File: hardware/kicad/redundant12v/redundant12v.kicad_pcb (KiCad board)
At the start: 2 copper layers, 66.7 x 26.4 mm, 30 parts, among them J1 Conn_01x06, J2 IDC 2x5 Male, Q1 2N3904, Q2 2N3904, U1 ATtiny212-SS, U2 MAX232CPE, U3 LD1117S50TR_SOT223, X1 ASCO

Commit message: Replace Maxim MAX232ECWE+T with TI MAX232EID for narrower SOIC-16
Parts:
- C1, C2, C4, C8: value C_Small -> 0.1μF
- C3, C5, C6, C7: value C_Small -> 1μF
- C9: value C_Small -> 10μF
- D1: value BZX84Cxx -> BZX84-A15,215
- F1: value Fuse -> F1206B1R00FSTR
- J1: value Conn_01x06 -> 22-12-2064
- Q1, Q2: value 2N3904 -> SMMBT3904LT1G
- U1: value ATtiny212-SS -> ATTINY212-SSF
- U2: value MAX232CPE -> TI MAX232EID
- U3: value LD1117S50TR_SOT223 -> LD1117S50CTR
- X1: value ASCO -> ECS-3951M-018-AU-TR
- renumbered TP1 to TP3
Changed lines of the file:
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@@
       (effects (font (size 1 1) (thickness 0.15)))
     )
-    (fp_text value "C_Small" (at -4.625 -1.27 90) (layer "F.Fab")
+    (fp_text value "0.1μF" (at -4.625 -1.27 90) (layer "F.Fab")
       (effects (font (size 1 1) (thickness 0.15)))
     )
@@
       (effects (font (size 1 1) (thickness 0.15)))
     )
-    (fp_text value "C_Small" (at -1.2935 1.172) (layer "F.Fab")
+    (fp_text value "10μF" (at -1.2935 1.172) (layer "F.Fab")
       (effects (font (size 1 1) (thickness 0.15)))
     )
@@
       (effects (font (size 1 1) (thickness 0.15)))
     )
-    (fp_text value "C_Small" (at 0 1.68 90) (layer "F.Fab")
+    (fp_text value "1μF" (at 0 1.68 90) (layer "F.Fab")
       (effects (font (size 1 1) (thickness 0.15)))
     )
@@
       (effects (font (size 1 1) (thickness 0.15)))
     )
-    (fp_text value "Conn_01x06" (at 6.25 3.4 90) (layer "F.Fab")
+    (fp_text value "22-12-2064" (at 6.25 3.4 90) (layer "F.Fab")
       (effects (font (size 1 1) (thickness 0.15)))
     )
@@
       (effects (font (size 1 1) (thickness 0.15)))
     )
-    (fp_text value "C_Small" (at -0.27 -2.54 90) (layer "F.Fab")
+    (fp_text value "1μF" (at -0.27 -2.54 90) (layer "F.Fab")
       (effects (font (size 1 1) (thickness 0.15)))
     )
@@
       (effects (font (size 1 1) (thickness 0.15)))
     )
-    (fp_text value "Fuse" (at -0.4207 5.376) (layer "F.Fab")
+    (fp_text value "F1206B1R00FSTR" (at -0.4207 5.376) (layer "F.Fab")
       (effects (font (size 1 1) (thickness 0.15)))
     )
@@
       (effects (font (size 1 1) (thickness 0.15)))
     )
-    (fp_text value "2N3904" (at -2.866 0.293 90) (layer "F.Fab")
+    (fp_text value "SMMBT3904LT1G" (at -2.866 0.293 90) (layer "F.Fab")
       (effects (font (size 1 1) (thickness 0.15)))
     )
@@
       (effects (font (size 1 1) (thickness 0.15)))
     )
-    (fp_text value "ATtiny212-SS" (at 0 3.4 90) (layer "F.Fab")
+    (fp_text value "ATTINY212-SSF" (at 0 3.4 90) (layer "F.Fab")
       (effects (font (size 1 1) (thickness 0.15)))
     )
@@
       (effects (font (size 1 1) (thickness 0.15)))
     )
-    (fp_text value "MAX232CPE" (at 0 10.1285 90) (layer "F.Fab")
+    (fp_text value "TI MAX232EID" (at 0 10.1285 90) (layer "F.Fab")
       (effects (font (size 1 1) (thickness 0.15)))
     )
@@
       (effects (font (size 1 1) (thickness 0.15)))
     )
-    (fp_text value "ASCO" (at 0 5 90) (layer "F.Fab")
+    (fp_text value "ECS-3951M-018-AU-TR" (at 0 5 90) (layer "F.Fab")
       (effects (font (size 1 1) (thickness 0.15)))
     )
@@
       (effects (font (size 1 1) (thickness 0.15)))
     )
-    (fp_text value "LD1117S50TR_SOT223" (at 0.127 -5.334 90) (layer "F.Fab")
+    (fp_text value "LD1117S50CTR" (at 0.127 -5.334 90) (layer "F.Fab")
       (effects (font (size 1 1) (thickness 0.15)))
     )
@@
       (effects (font (size 1 1) (thickness 0.15)))
     )
-    (fp_text value "C_Small" (at -4.18 -12.9325) (layer "F.Fab")
+    (fp_text value "1μF" (at -4.18 -12.9325) (layer "F.Fab")
       (effects (font (size 1 1) (thickness 0.15)))
     )
@@
       (effects (font (size 1 1) (thickness 0.15)))
     )
-    (fp_text value "C_Small" (at -1.188 -2.8045 90) (layer "F.Fab")
+    (fp_text value "0.1μF" (at -1.188 -2.8045 90) (layer "F.Fab")
       (effects (font (size 1 1) (thickness 0.15)))
     )
@@
       (effects (font (size 1 1) (thickness 0.15)))
     )
-    (fp_text value "C_Small" (at 0 1.68 90) (layer "F.Fab")
+    (fp_text value "0.1μF" (at 0 1.68 90) (layer "F.Fab")
       (effects (font (size 1 1) (thickness 0.15)))
     )
@@
       (effects (font (size 1 1) (thickness 0.15)))
     )
-    (fp_text value "BZX84Cxx" (at 0 2.4 90) (layer "F.Fab")
+    (fp_text value "BZX84-A15,215" (at 0 2.4 90) (layer "F.Fab")
       (effects (font (size 1 1) (thickness 0.15)))
     )
@@
       (effects (font (size 1 1) (thickness 0.15)))
     )
-    (fp_text value "C_Small" (at 2.7755 1.742 90) (layer "F.Fab")
+    (fp_text value "1μF" (at 2.7755 1.742 90) (layer "F.Fab")
       (effects (font (size 1 1) (thickness 0.15)))
     )
@@
       (effects (font (size 1 1) (thickness 0.15)))
     )
-    (fp_text value "C_Small" (at -0.115 -0.559 90) (layer "F.Fab")
+    (fp_text value "0.1μF" (at -0.115 -0.559 90) (layer "F.Fab")
       (effects (font (size 1 1) (thickness 0.15)))
     )
@@
       (effects (font (size 1 1) (thickness 0.15)))
     )
-    (fp_text value "2N3904" (at 4.157 3.826) (layer "F.Fab")
+    (fp_text value "SMMBT3904LT1G" (at 4.157 3.826) (layer "F.Fab")
       (effects (font (size 1 1) (thickness 0.15)))
     )
@@
     (property "Sheetname" "")
     (attr exclude_from_pos_files)
-    (fp_text reference "TP1" (at 0 2.148) (layer "B.SilkS") hide
+    (fp_text reference "TP3" (at 0 2.148) (layer "B.SilkS") hide
       (effects (font (size 1 1) (thickness 0.15)) (justify mirror))
     )

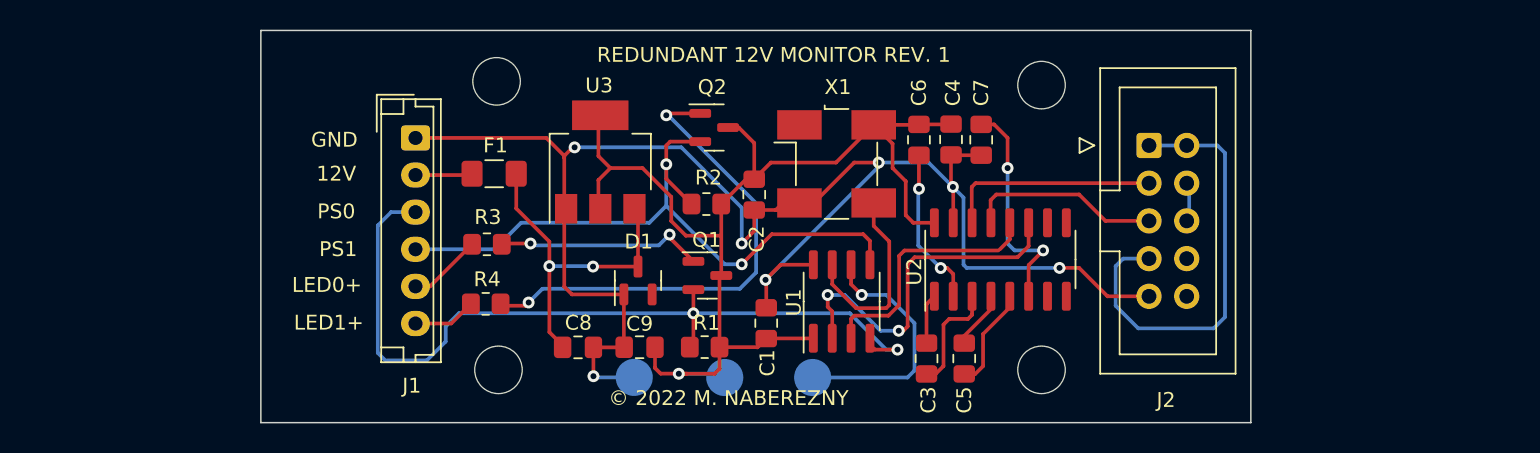
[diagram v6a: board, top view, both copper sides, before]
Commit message: Fix alarm detection, rotate serial connector
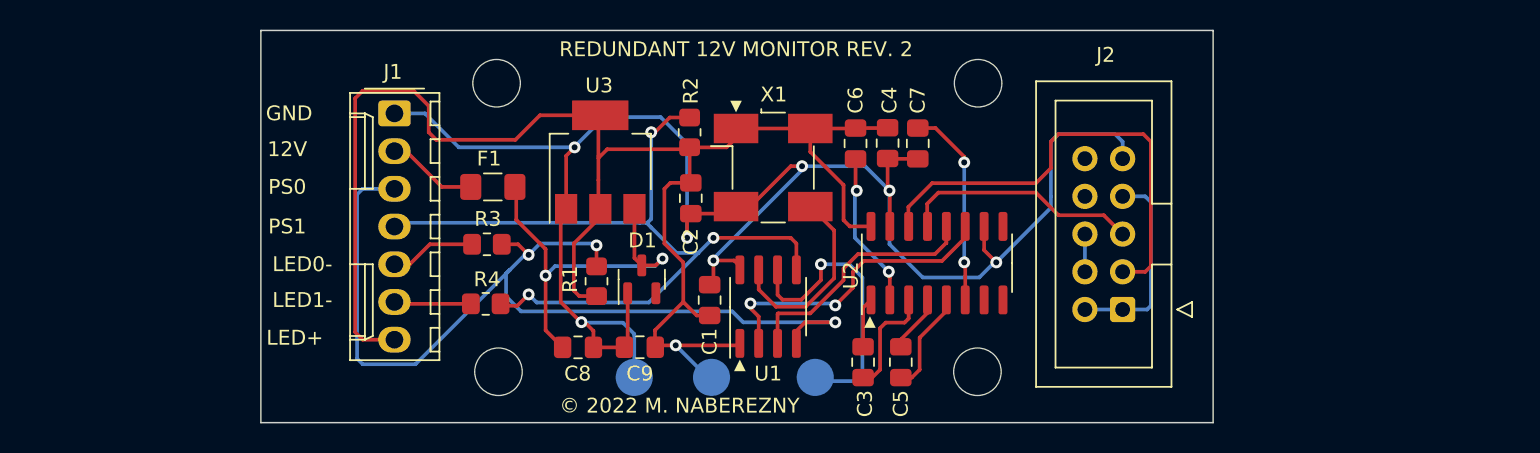
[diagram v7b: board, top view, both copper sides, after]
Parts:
- removed Q1, Q2: SMMBT3904LT1G, Package_TO_SOT_SMD:SOT-23
- J1: value 22-12-2064 -> Conn_01x07; footprint Connector_JST:JST_EH_B6B-EH-A_1x06_P2.50mm_Vertical -> Connector_Molex:Molex_KK-254_AE-6410-07A_1x07_P2.54mm_Vertical
- moved J2 11.2 mm to (176.1, 99.1), turned to 180 degrees
- moved R1 8.53 mm to (140.7, 97.2), turned to 90 degrees
- moved U1 4.97 mm to (152.3, 98.9)
- moved R2 4.96 mm to (147.0, 87.1), turned to 90 degrees
- moved REF** 4.32 mm to (166.4, 103.3)
- moved C3 4.28 mm to (158.7, 102.6)
- moved U2 4.28 mm to (163.6, 95.9)
- moved C4 4.28 mm to (160.3, 87.9)
- moved C5 4.28 mm to (161.2, 102.6)
- moved C6 4.28 mm to (158.2, 87.9)
- moved C7 4.28 mm to (162.4, 87.9)
- moved X1 4.28 mm to (152.6, 89.5)
- moved C2 4.28 mm to (147.1, 91.6)
- moved REF** 4.27 mm to (166.4, 83.8)
- moved C1 4.11 mm to (148.3, 98.4)
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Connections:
- net LED0+ renamed LED0-
- net LED1+ renamed LED1-
- R3 pad 1: Net-(Q1-Pad1) -> PS0
- R4 pad 1: Net-(Q2-Pad1) -> PS1
- U2 pad 10: unconnected-(U2-Pad10) -> GND
- X1 pad 1: unconnected-(X1-Pad1) -> VCC
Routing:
- net VCC: track 77.3 -> 111.1 mm
- net Net-(Q2-Pad1): track 33.7 -> 0.00 mm, vias 2 -> 0
- net TX_12V: track 14.5 -> 31.4 mm
- net Net-(J2-Pad1): track 29.8 -> 13.6 mm
- net Net-(Q1-Pad1): track 14.2 -> 0.00 mm, vias 2 -> 0
- net GND: track 111.7 -> 123.6 mm
- net PS0: track 55.9 -> 65.4 mm, vias 2 -> 3
- net PS1: track 45.9 -> 54.9 mm, vias 2 -> 3
- net TX_5V: track 24.0 -> 20.7 mm
- net Net-(C8-Pad2): track 23.0 -> 26.1 mm
- net RX_12V: track 13.1 -> 16.2 mm
- net UPDI: track 16.9 -> 19.2 mm
- net Net-(C7-Pad2): track 15.3 -> 13.6 mm
- net 12V: track 4.74 -> 6.14 mm
- net LED1-: track 4.28 -> 5.20 mm
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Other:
- board size 66.7 x 26.4 mm -> 64.1 x 26.4 mm
- board text added: "LED+"
- board text added: "LED0-"
- board text added: "LED1-"
- board text added: "REDUNDANT 12V MONITOR REV. 2"
- board text added: "▲"
- board text removed: "LED0+"
- board text removed: "LED1+"
- board text removed: "REDUNDANT 12V MONITOR REV. 1"

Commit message: Increase width of all traces, widen board under Molex connector
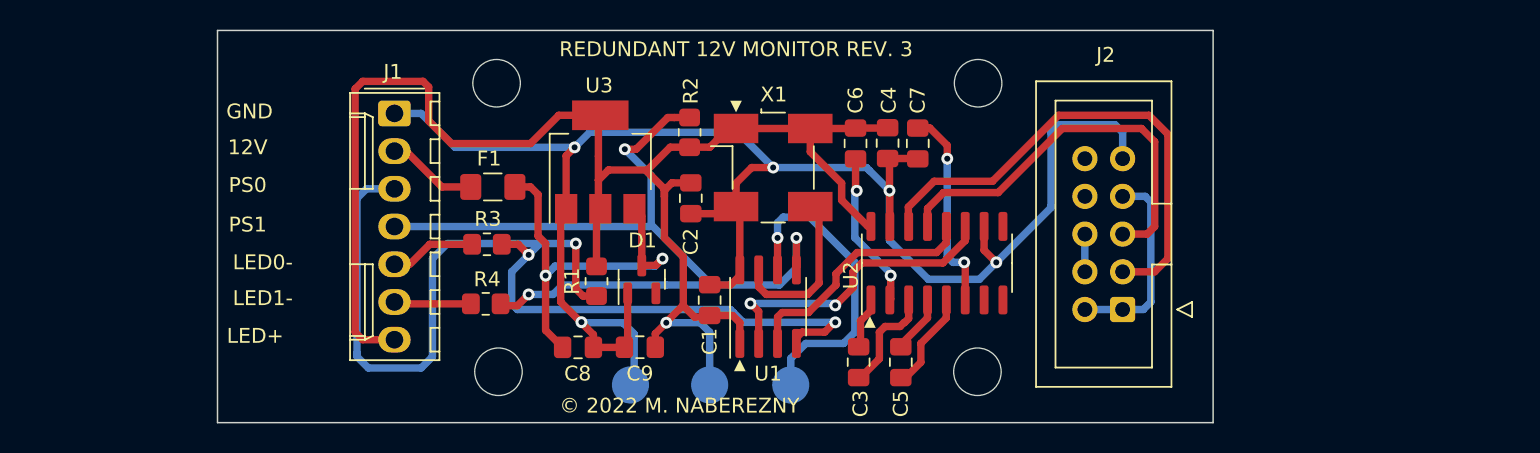
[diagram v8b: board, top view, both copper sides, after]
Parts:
- moved TP2 1.73 mm to (153.8, 104.1)
- moved TP3 0.57 mm to (143.0, 104.1)
- moved TP1 0.52 mm to (148.3, 104.1)
- moved C3 0.30 mm to (158.4, 102.6)
- turned R1 to -90 degrees
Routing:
- net RX_12V: track 16.2 -> 27.2 mm
- net PS0: track 65.4 -> 74.4 mm
- net GND: track 123.6 -> 117.0 mm, vias 7 -> 5
- net PS1: track 54.9 -> 59.5 mm
- net TX_12V: track 31.4 -> 33.7 mm
- net UPDI: track 19.2 -> 21.3 mm
- net VCC: track 111.1 -> 109.0 mm
- net EXTCLK: track 13.2 -> 11.1 mm
- net TX_5V: track 20.7 -> 21.6 mm
- net Net-(C5-Pad1): track 3.90 -> 4.77 mm
- net Net-(C8-Pad2): track 26.1 -> 26.7 mm
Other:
- board size 64.1 x 26.4 mm -> 67.1 x 26.4 mm
- board text added: "REDUNDANT 12V MONITOR REV. 3"
- board text removed: "REDUNDANT 12V MONITOR REV. 2"
